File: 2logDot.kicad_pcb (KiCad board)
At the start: 4 copper layers, 66 x 66 mm, 8 parts, among them J1 RFID, J2 NEOPIXEL_RING, J3 Conn_01x14_Male, J4 Conn_01x13_Male, SW1 SOFT_RESET, U1 mini_esp32

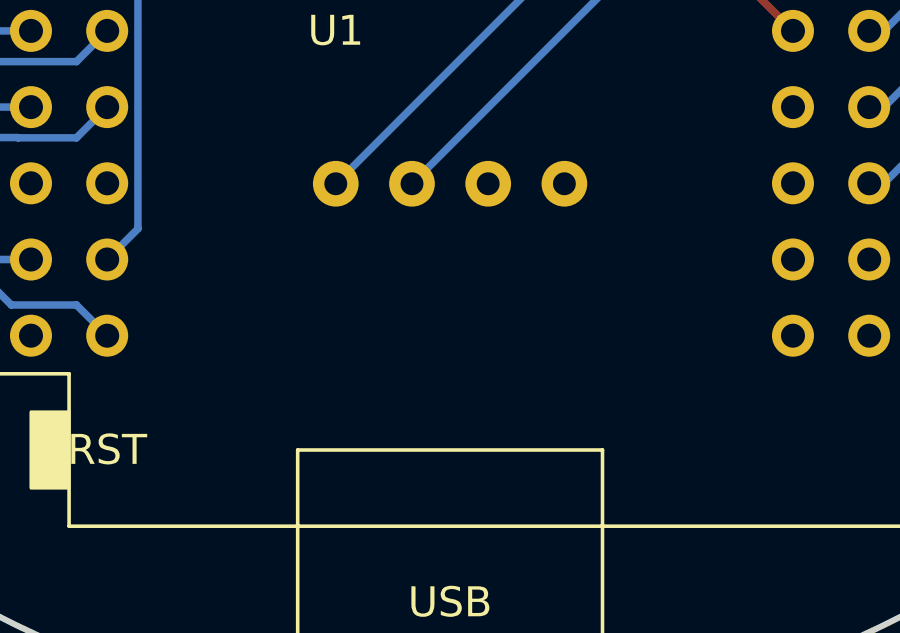
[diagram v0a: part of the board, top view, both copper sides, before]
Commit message: added oled header
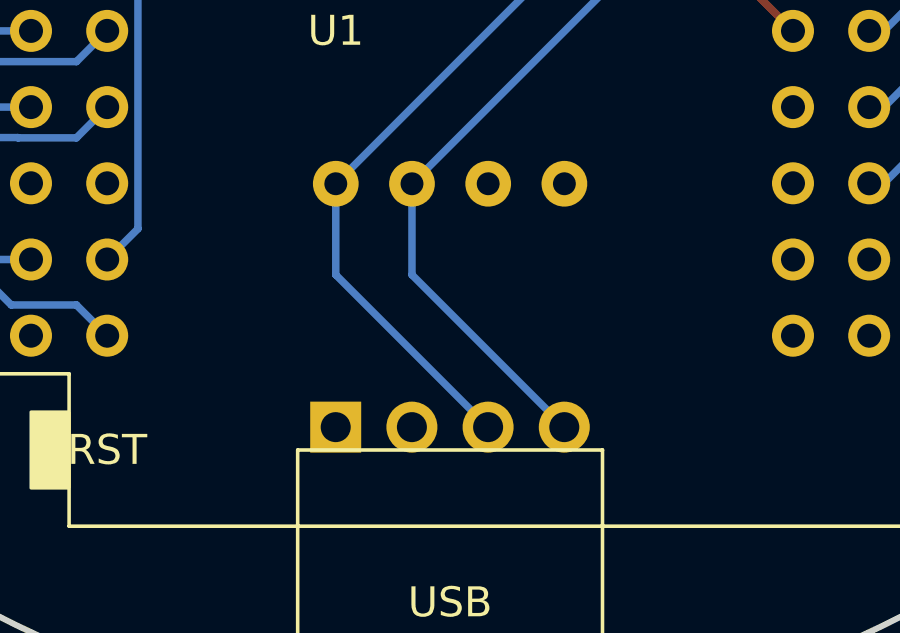
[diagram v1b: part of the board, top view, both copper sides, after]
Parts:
- added J5: I2C_OLED, Connector_PinHeader_2.54mm:PinHeader_1x04_P2.54mm_Vertical, B.Cu at (146.2, 123.1)
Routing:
- net /SCL: track 33.3 -> 43.5 mm
- net /SDA: track 29.7 -> 39.9 mm
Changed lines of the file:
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@@
+    )
+  )
+  (footprint "Connector_PinHeader_2.54mm:PinHeader_1x04_P2.54mm_Vertical" (layer "B.Cu")
+    (at 146.187 123.063 -90)
+    (descr "Through hole straight pin header, 1x04, 2.54mm pitch, single row")
+    (tags "Through hole pin header THT 1x04 2.54mm single row")
+    (property "Sheetfile" "2logDot.kicad_sch")
+    (property "Sheetname" "")
+    (attr through_hole)
+    (fp_text reference "J5" (at 0 2.804 180) (layer "B.SilkS")
+      (effects (font (size 1 1) (thickness 0.15)) (justify mirror))
+    )
+    (fp_text value "I2C_OLED" (at 0 -9.95 90) (layer "B.Fab")
+      (effects (font (size 1 1) (thickness 0.15)) (justify mirror))
+    )
+    (fp_text user "${REFERENCE}" (at 0 -3.81) (layer "B.Fab")
+      (effects (font (size 1 1) (thickness 0.15)) (justify mirror))
+    )
+    (fp_line (start -1.33 1.33) (end 0 1.33) (layer "B.SilkS") (width 0.12))
+    (fp_line (start -1.33 -8.95) (end 1.33 -8.95) (layer "B.SilkS") (width 0.12))
+    (fp_line (start -1.33 0) (end -1.33 1.33) (layer "B.SilkS") (width 0.12))
+    (fp_line (start -1.33 -1.27) (end 1.33 -1.27) (layer "B.SilkS") (width 0.12))
+    (fp_line (start -1.33 -1.27) (end -1.33 -8.95) (layer "B.SilkS") (width 0.12))
+    (fp_line (start 1.33 -1.27) (end 1.33 -8.95) (layer "B.SilkS") (width 0.12))
+    (fp_line (start 1.8 -9.4) (end 1.8 1.8) (layer "B.CrtYd") (width 0.05))
+    (fp_line (start 1.8 1.8) (end -1.8 1.8) (layer "B.CrtYd") (width 0.05))
+    (fp_line (start -1.8 -9.4) (end 1.8 -9.4) (layer "B.CrtYd") (width 0.05))
+    (fp_line (start -1.8 1.8) (end -1.8 -9.4) (layer "B.CrtYd") (width 0.05))
+    (fp_line (start -1.27 -8.89) (end -1.27 0.635) (layer "B.Fab") (width 0.1))
+    (fp_line (start 1.27 -8.89) (end -1.27 -8.89) (layer "B.Fab") (width 0.1))
+    (fp_line (start 1.27 1.27) (end 1.27 -8.89) (layer "B.Fab") (width 0.1))
+    (fp_line (start -1.27 0.635) (end -0.635 1.27) (layer "B.Fab") (width 0.1))
+    (fp_line (start -0.635 1.27) (end 1.27 1.27) (layer "B.Fab") (width 0.1))
+    (pad "1" thru_hole rect locked (at 0 0 270) (size 1.7 1.7) (drill 1) (layers *.Cu *.Mask)
+      (net 2 "GND") (pinfunction "Pin_1") (pintype "passive"))
+    (pad "2" thru_hole oval locked (at 0 -2.54 270) (size 1.7 1.7) (drill 1) (layers *.Cu *.Mask)
+      (net 5 "+5V") (pinfunction "Pin_2") (pintype "passive"))
+    (pad "3" thru_hole oval locked (at 0 -5.08 270) (size 1.7 1.7) (drill 1) (layers *.Cu *.Mask)
+      (net 3 "/SCL") (pinfunction "Pin_3") (pintype "passive"))
+    (pad "4" thru_hole oval locked (at 0 -7.62 270) (size 1.7 1.7) (drill 1) (layers *.Cu *.Mask)
+      (net 4 "/SDA") (pinfunction "Pin_4") (pintype "passive"))
+    (model "${KICAD6_3DMODEL_DIR}/Connector_PinHeader_2.54mm.3dshapes/PinHeader_1x04_P2.54mm_Vertical.wrl"
+      (offset (xyz 0 0 0))
+      (scale (xyz 1 1 1))
+      (rotate (xyz 0 0 0))
     )
   )
@@
   (gr_rect (start 183.25 94.5) (end 178.25 108.5) (layer "Dwgs.User") (width 0.2) (fill none))
   (gr_circle (center 150 100) (end 183 100) (layer "Edge.Cuts") (width 0.2) (fill none))
+  (gr_text "GND" (at 146.304 125.984 90) (layer "B.SilkS")
+    (effects (font (size 1 1) (thickness 0.15)) (justify mirror))
+  )
+  (gr_text "GND" (at 153.797 117.602 90) (layer "B.SilkS")
+    (effects (font (size 1 1) (thickness 0.15)) (justify mirror))
+  )
+  (gr_text "SDA" (at 148.717 117.348 90) (layer "B.SilkS")
+    (effects (font (size 1 1) (thickness 0.15)) (justify mirror))
+  )
+  (gr_text "SCL" (at 151.257 125.984 90) (layer "B.SilkS")
+    (effects (font (size 1 1) (thickness 0.15)) (justify mirror))
+  )
+  (gr_text "5V" (at 151.384 117.221 90) (layer "B.SilkS")
+    (effects (font (size 1 1) (thickness 0.15)) (justify mirror))
+  )
+  (gr_text "5V" (at 148.844 125.984 90) (layer "B.SilkS")
+    (effects (font (size 1 1) (thickness 0.15)) (justify mirror))
+  )
   (gr_text "IN" (at 177.165 104.14) (layer "B.SilkS")
     (effects (font (size 1.5 1.5) (thickness 0.3)) (justify mirror))
   )
+  (gr_text "SDA" (at 153.924 125.984 90) (layer "B.SilkS")
+    (effects (font (size 1 1) (thickness 0.15)) (justify mirror))
+  )
   (gr_text "out" (at 177.8 101.6) (layer "B.SilkS")
     (effects (font (size 1 1) (thickness 0.25)) (justify mirror))
@@
   (gr_text "5V" (at 177.8 98.425) (layer "B.SilkS")
     (effects (font (size 1 1) (thickness 0.25)) (justify mirror))
+  )
+  (gr_text "SCL" (at 146.177 117.348 90) (layer "B.SilkS")
+    (effects (font (size 1 1) (thickness 0.15)) (justify mirror))
   )
   (gr_text "LED" (at 166.37 88.9) (layer "F.SilkS")
@@
   (segment (start 168.5 96.75) (end 168.5 95.66) (width 0.25) (layer "B.Cu") (net 3))
   (segment (start 164.530489 100.719511) (end 168.5 96.75) (width 0.25) (layer "B.Cu") (net 3))
+  (segment (start 146.19 117.986) (end 151.267 123.063) (width 0.25) (layer "B.Cu") (net 3))
   (segment (start 168.5 95.66) (end 170.18 93.98) (width 0.25) (layer "B.Cu") (net 3))
   (segment (start 162.945489 100.719511) (end 164.530489 100.719511) (width 0.25) (layer "B.Cu") (net 3))
+  (segment (start 146.19 114.95) (end 146.19 117.986) (width 0.25) (layer "B.Cu") (net 3))
   (segment (start 161.43 102.235) (end 162.945489 100.719511) (width 0.25) (layer "B.Cu") (net 3))
   (segment (start 158.905 102.235) (end 161.43 102.235) (width 0.25) (layer "B.Cu") (net 3))
   (segment (start 146.19 114.95) (end 158.905 102.235) (width 0.25) (layer "B.Cu") (net 3))
   (segment (start 168.5 98.2) (end 170.18 96.52) (width 0.25) (layer "B.Cu") (net 4))
+  (segment (start 148.73 114.95) (end 148.73 117.986) (width 0.25) (layer "B.Cu") (net 4))
+  (segment (start 148.73 117.986) (end 153.807 123.063) (width 0.25) (layer "B.Cu") (net 4))
   (segment (start 164.490489 103.259511) (end 168.5 99.25) (width 0.25) (layer "B.Cu") (net 4))
   (segment (start 162.945489 103.259511) (end 164.490489 103.259511) (width 0.25) (layer "B.Cu") (net 4))

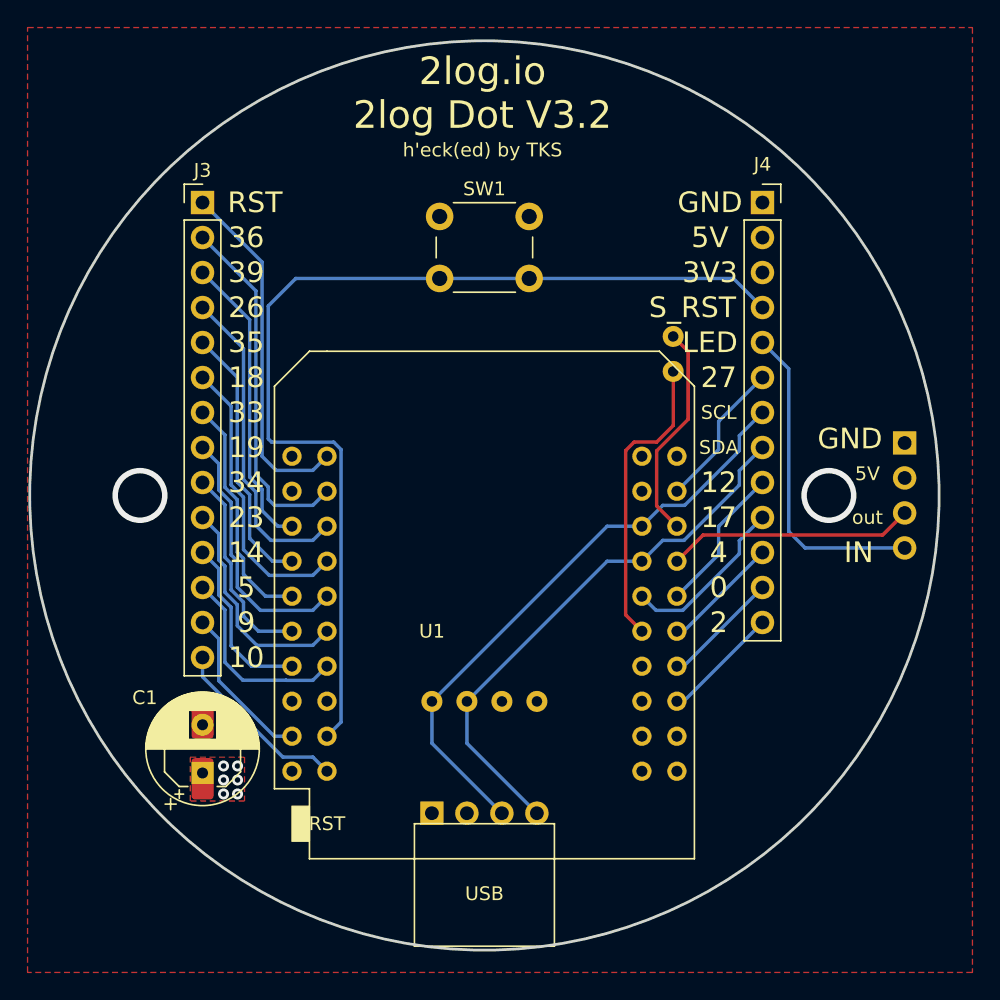
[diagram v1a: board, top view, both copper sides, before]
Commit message: flipped display to be able to center the screen
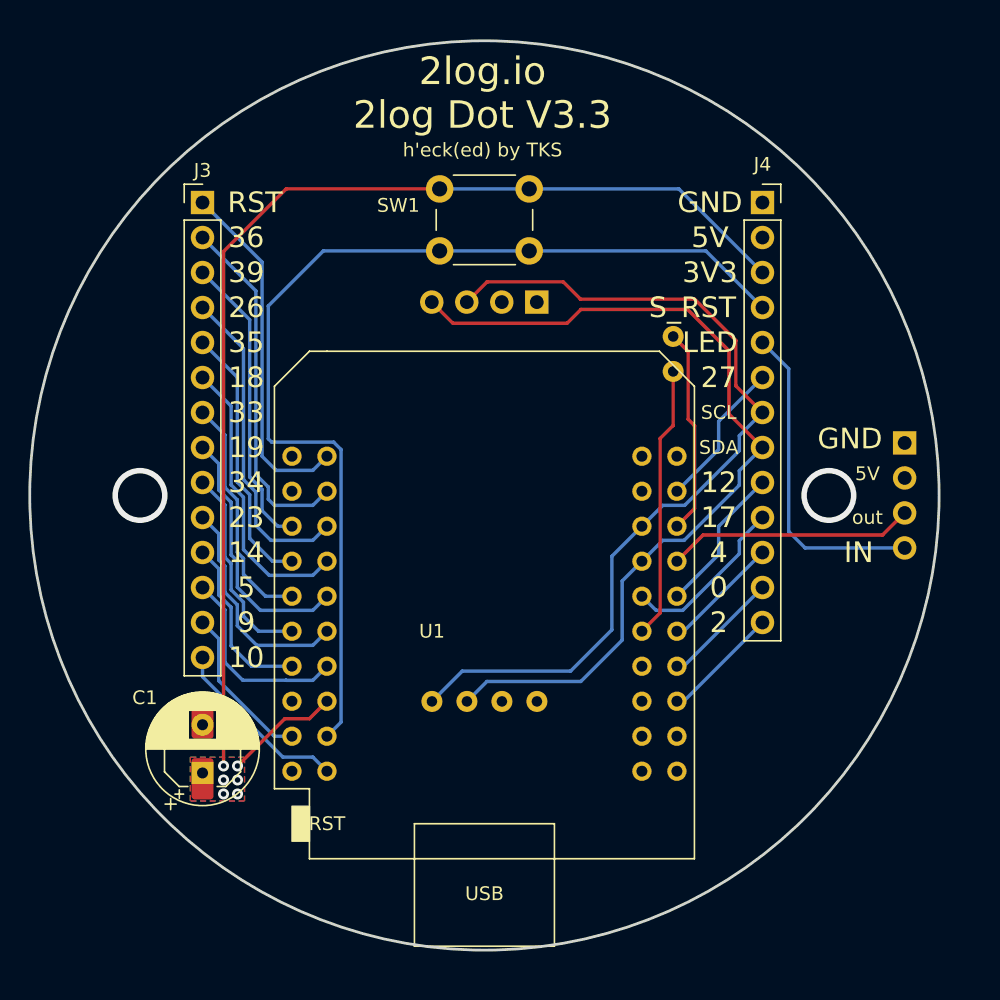
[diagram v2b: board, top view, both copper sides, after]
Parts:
- moved J5 37.9 mm to (153.8, 86.0), turned to 90 degrees
- moved SW1 2.00 mm to (146.8, 77.8)
- renumbered REF** to C1_ALT
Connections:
- C1_ALT pad 1: (no net) -> +3V3
- C1_ALT pad 2: (no net) -> GND
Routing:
- net GND: track 0.00 -> 189.2 mm
- net +5V: track 0.00 -> 111.0 mm
- net +3V3: track 0.00 -> 89.3 mm
- net /SDA: track 39.9 -> 64.1 mm
- net /SCL: track 43.5 -> 64.4 mm
- net /NFC_IRQ: track 21.9 -> 19.8 mm
- net /S_RES: track 73.6 -> 75.3 mm
- net /NRF_RST: track 15.8 -> 14.9 mm
- added copper zone on B.Cu, net +3V3
- removed copper zone on In2.Cu, net +3V3
- removed copper zone on In1.Cu, net +5V
- removed copper zone on F.Cu, net GND
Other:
- board text added: "2log Dot V3.3"
- board text removed: "2log Dot V3.2"
